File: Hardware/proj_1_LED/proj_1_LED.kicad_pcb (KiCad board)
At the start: 2 copper layers, 15.5 x 26 mm, 6 parts, among them J1 Conn_01x02, SW1 SW_Push

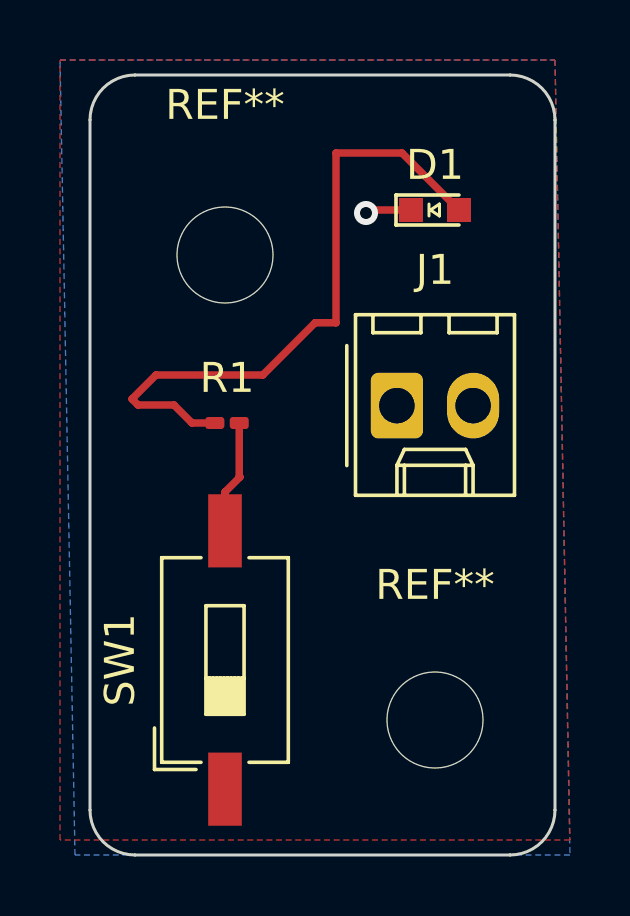
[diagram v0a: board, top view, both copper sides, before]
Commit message: Fix unnecessary wire bends on hardware traces
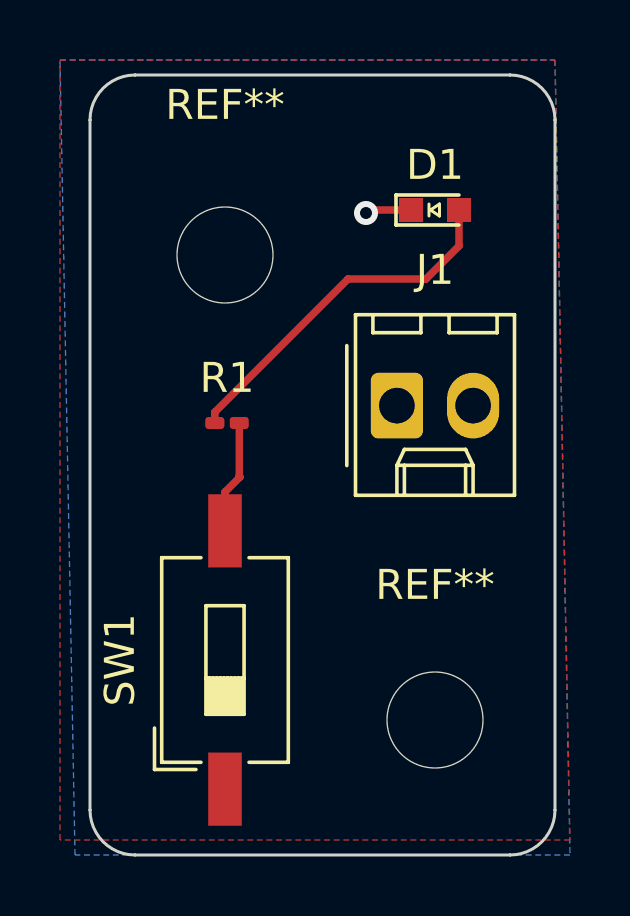
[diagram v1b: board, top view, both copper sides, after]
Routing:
- net Net-(D1-A): track 21.5 -> 12.0 mm
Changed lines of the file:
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@@
 	)
 	(segment
-		(start 34.6 34)
-		(end 35.8 34)
+		(start 44.2 29.8)
+		(end 41.6 29.8)
 		(width 0.25)
 		(layer "F.Cu")
@@
 	)
 	(segment
-		(start 43.4 25.6)
-		(end 41.2 25.6)
+		(start 41.6 29.8)
+		(end 37.16 34.24)
 		(width 0.25)
 		(layer "F.Cu")
@@
 	)
 	(segment
-		(start 35.2 33)
-		(end 34.4 33.8)
+		(start 45.3 28.7)
+		(end 44.2 29.8)
 		(width 0.25)
 		(layer "F.Cu")
@@
 	)
 	(segment
-		(start 38.760001 33)
-		(end 35.2 33)
-		(width 0.25)
-		(layer "F.Cu")
-		(net 2)
-	)
-	(segment
-		(start 36.4 34.6)
+		(start 37.16 34.24)
 		(end 37.16 34.6)
 		(width 0.25)
@@
 	)
 	(segment
-		(start 40.5 31.260001)
-		(end 38.760001 33)
+		(start 45.3 27.5)
+		(end 45.3 28.7)
 		(width 0.25)
 		(layer "F.Cu")
-		(net 2)
-	)
-	(segment
-		(start 34.4 33.8)
-		(end 34.6 34)
-		(width 0.25)
-		(layer "F.Cu")
-		(net 2)
-	)
-	(segment
-		(start 35.8 34)
-		(end 36.4 34.6)
-		(width 0.25)
-		(layer "F.Cu")
-		(net 2)
-	)
-	(segment
-		(start 45.3 27.5)
-		(end 43.4 25.6)
-		(width 0.25)
-		(layer "F.Cu")
-		(net 2)
-	)
-	(segment
-		(start 41.2 31.260001)
-		(end 40.5 31.260001)
-		(width 0.25)
-		(layer "F.Cu")
-		(net 2)
-	)
-	(segment
-		(start 41.2 25.6)
-		(end 41.2 31.260001)
-		(width 0.25)
-		(layer "F.Cu")
